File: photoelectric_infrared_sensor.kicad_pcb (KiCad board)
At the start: 4 copper layers, 121.1 x 63 mm, 38 parts

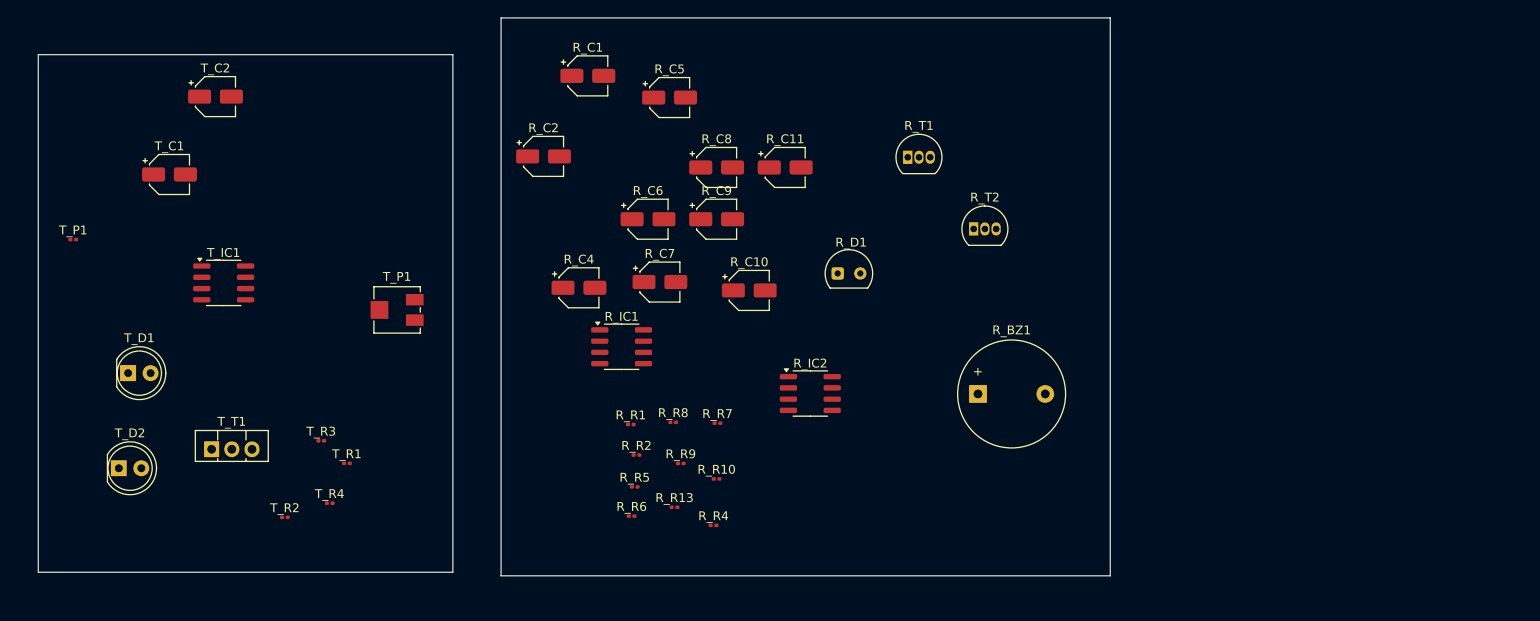
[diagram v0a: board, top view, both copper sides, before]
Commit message: added BOM
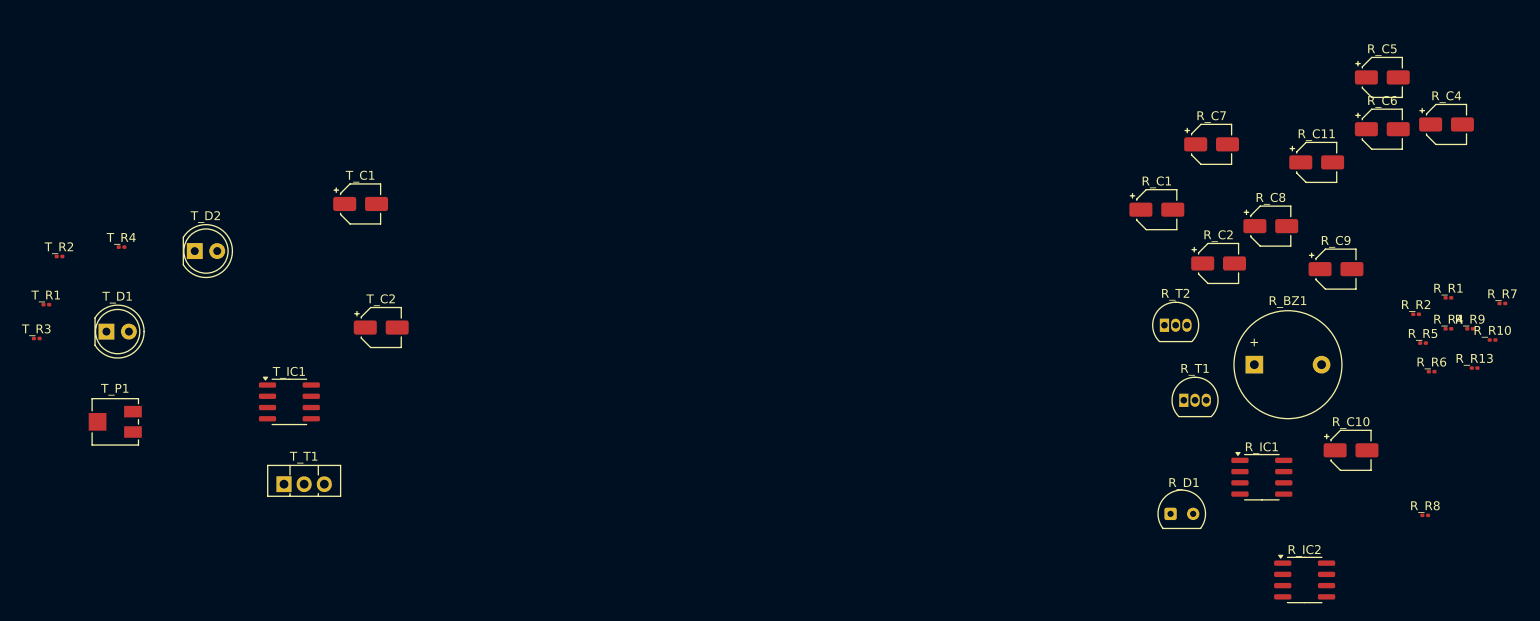
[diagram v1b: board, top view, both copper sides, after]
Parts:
- removed the T_P1 at (21.1, 58.5)
- removed the T_P1 at (57.8, 66.5)
- added T_P1: 10k, Potentiometer_SMD:Potentiometer_Vishay_TS53YJ_Vertical, F.Cu at (25.9, 79.2)
- R_IC1: value NE567 -> NE567_custom
- R_IC2: value NE555D -> NE555D_custom
- T_IC1: value TLC555xD -> TLC555xD_custom
- moved R_C4 99.8 mm to (176.3, 45.5)
- moved R_R1 93.5 mm to (176.6, 65.1)
- moved R_R6 91.9 mm to (174.7, 73.5)
- moved R_R13 91.8 mm to (179.5, 73.1)
- moved R_R5 90.6 mm to (173.7, 70.2)
- moved R_R9 90.5 mm to (179.0, 68.6)
- moved R_R7 89.7 mm to (182.7, 65.8)
- moved R_R2 89.5 mm to (172.9, 67.0)
- moved R_R10 89.1 mm to (181.6, 69.9)
- moved R_R4 86.0 mm to (176.6, 68.6)
- moved R_R8 85.6 mm to (173.9, 89.7)
- moved R_C6 83.6 mm to (169.1, 46.1)
- moved R_C5 80.6 mm to (169.1, 40.2)
- moved R_C2 77.2 mm to (150.6, 61.2)
- moved R_IC1 73.8 mm to (155.5, 85.4)
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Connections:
- net Net-(R_D1-K) renamed /R_LED
- net Net-(R_IC1-C3) renamed /R_C3
- net Net-(R_IC1-RC) renamed /R_RC
- net Net-(R_IC2-DIS) renamed /R_DIS
- net Net-(R_T1-C) renamed /R_BASE2
- net Net-(R_T2-E) renamed /R_EMITTER2
- net Net-(T_D1-A) renamed /T_LED1
- net Net-(T_D1-K) renamed /T_LED2
- net Net-(T_T1-B) renamed /T_BASE
- net Net-(T_T1-C) renamed /T_EMITTER
- net R_C2 renamed /R_C2
- net R_CV renamed /R_CV
- net R_IN renamed /R_IN
- net R_OUT1 renamed /R_OUT1
- net R_OUT2 renamed /R_OUT2
- net R_R renamed /R_R
- net R_TR renamed /R_THR/TR
- net T_DIS renamed /T_DIS
- net T_OUT renamed /T_OUT
- net T_THR renamed /T_THR/TR
- T_R1 pad 2: Net-(T_P1-Pad1) -> /T_POT
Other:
- board outline removed

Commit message: finished schematics
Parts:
- R_BZ1: footprint Buzzer_Beeper:Buzzer_12x9.5RM7.6 -> CPT-1203-03-SMT-TR:CPT-1203-03-SMT-TR
- R_C1, R_C10, R_C2, R_C4, R_C5, R_C8, R_C9, T_C1: footprint Capacitor_SMD:CP_Elec_4x3 -> Capacitor_SMD:C_0402_1005Metric_Pad0.74x0.62mm_HandSolder
- R_D1: value SFH205F -> BPW34; footprint OptoDevice:Osram_SFH205 -> BPW_34_FAS-Z:BPW34FASZ
- R_R1, R_R10, R_R13, R_R2, R_R4, R_R5, R_R6, R_R7, R_R8, R_R9, T_R1, T_R2, T_R3: footprint Resistor_SMD:R_0201_0603Metric -> ERJUP6:ERJUP6
- T_C2: footprint Capacitor_SMD:CP_Elec_4x3 -> Capacitor_SMD:CP_Elec_3x5.4
- T_D1, T_D2: value LD271 -> SFH 4851; footprint LED_THT:LED_D5.0mm_IRGrey -> SFH_4851:SFH4851
- T_P1: value 10k -> PVG5A103C03R00; footprint Potentiometer_SMD:Potentiometer_Vishay_TS53YJ_Vertical -> PVG5A103C03R00:PVG5A100C03R00
- T_R4: footprint Resistor_SMD:R_0201_0603Metric -> ERJS1T_U1T__2512_:ERJS1T_U1T__2512_
- T_T1: value BD140 -> BD136
- moved R_IC2 81.9 mm to (242.0, 91.0)
- moved R_IC1 74.0 mm to (229.3, 91.1)
- moved T_IC1 55.0 mm to (100.5, 78.7)
- moved T_R4 50.7 mm to (71.5, 82.9)
- moved T_P1 37.3 mm to (61.9, 88.8)
- moved R_BZ1 35.7 mm to (190.3, 73.6)
- moved T_D1 35.4 mm to (59.5, 76.3)
- moved T_D2 35.1 mm to (68.4, 70.0)
- moved R_C4 31.6 mm to (207.0, 53.2)
- moved R_D1 31.6 mm to (175.8, 97.2)
- moved R_R2 31.6 mm to (203.6, 74.7)
- moved R_R5 31.6 mm to (204.4, 78.0)
- moved R_R6 31.6 mm to (205.3, 81.2)
- moved R_R7 31.6 mm to (213.3, 73.5)
- moved R_R8 31.6 mm to (204.6, 97.4)
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
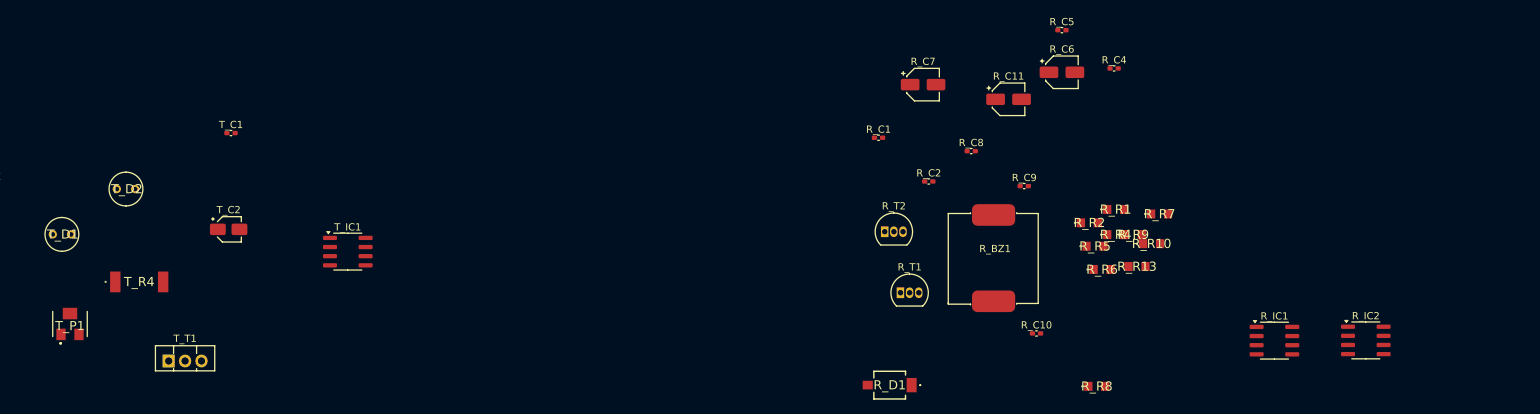
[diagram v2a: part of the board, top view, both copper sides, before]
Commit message: added schematics as .pdf
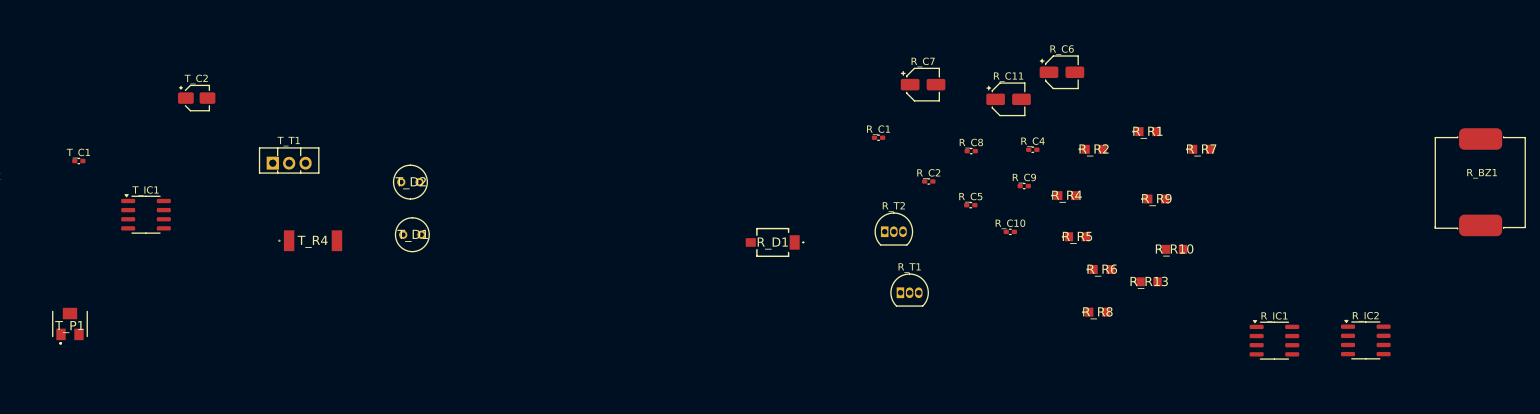
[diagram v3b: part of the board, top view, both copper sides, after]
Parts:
- moved R_BZ1 68.5 mm to (257.9, 63.0)
- moved T_D1 48.7 mm to (108.2, 76.3)
- moved T_D2 39.5 mm to (108.0, 69.0)
- moved T_T1 31.1 mm to (90.1, 66.4)
- moved T_IC1 28.5 mm to (72.5, 73.6)
- moved R_C5 27.4 mm to (187.1, 72.2)
- moved R_D1 25.6 mm to (159.6, 77.4)
- moved T_R4 24.8 mm to (95.7, 77.2)
- moved T_C1 21.5 mm to (63.2, 66.1)
- moved T_C2 18.8 mm to (79.5, 57.4)
- moved R_C4 16.0 mm to (195.7, 64.5)
- moved R_C10 14.6 mm to (192.6, 76.0)
- moved R_R1 11.7 mm to (211.7, 62.0)
- moved R_R7 10.7 mm to (219.2, 64.5)
- moved R_R8 10.3 mm to (204.7, 87.1)
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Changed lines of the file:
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@@
 	(footprint "ERJUP6:ERJUP6"
 		(layer "F.Cu")
-		(at 209.685 76.335)
+		(at 212.935 71.38)
 		(descr "ERJUP6")
 		(tags "Resistor")
@@
 	(footprint "ERJUP6:ERJUP6"
 		(layer "F.Cu")
-		(at 212.225 77.6)
+		(at 215.395 78.38)
 		(descr "ERJUP6")
 		(tags "Resistor")
@@
 	(footprint "ERJUP6:ERJUP6"
 		(layer "F.Cu")
-		(at 204.615 97.42)
+		(at 204.735 87.11)
 		(descr "ERJUP6")
 		(tags "Resistor")
@@
 	(footprint "Capacitor_SMD:C_0402_1005Metric_Pad0.74x0.62mm_HandSolder"
 		(layer "F.Cu")
-		(at 196.23 90.07)
+		(at 192.5925 75.95)
 		(descr "Capacitor SMD 0402 (1005 Metric), square (rectangular) end terminal, IPC_7351 nominal with elongated pad for handsoldering. (Body size source: IPC-SM-782 page 76, https://www.pcb-3d.com/wordpress/wp-content/uploads/ipc-sm-782a_amendment_1_and_2.pdf), generated with kicad-footprint-generator")
 		(tags "capacitor handsolder")
@@
 	(footprint "ERJUP6:ERJUP6"
 		(layer "F.Cu")
-		(at 213.335 73.47)
+		(at 219.175 64.48)
 		(descr "ERJUP6")
 		(tags "Resistor")
@@
 	(footprint "Capacitor_SMD:C_0402_1005Metric_Pad0.74x0.62mm_HandSolder"
 		(layer "F.Cu")
-		(at 84.295 62.225)
+		(at 63.1525 66.11)
 		(descr "Capacitor SMD 0402 (1005 Metric), square (rectangular) end terminal, IPC_7351 nominal with elongated pad for handsoldering. (Body size source: IPC-SM-782 page 76, https://www.pcb-3d.com/wordpress/wp-content/uploads/ipc-sm-782a_amendment_1_and_2.pdf), generated with kicad-footprint-generator")
 		(tags "capacitor handsolder")
@@
 	(footprint "ERJUP6:ERJUP6"
 		(layer "F.Cu")
-		(at 210.195 80.77)
+		(at 211.875 82.89)
 		(descr "ERJUP6")
 		(tags "Resistor")
@@
 	(footprint "Package_TO_SOT_THT:TO-126-3_Vertical"
 		(layer "F.Cu")
-		(at 75.635 93.895)
+		(at 90.1 66.41)
 		(descr "TO-126-3, Vertical, RM 2.28mm, see https://www.diodes.com/assets/Package-Files/TO126.pdf")
 		(tags "TO-126-3 Vertical RM 2.28mm")
@@
 	(footprint "SFH_4851:SFH4851"
 		(layer "F.Cu")
-		(at 68.43 70)
+		(at 107.96 69.04)
 		(descr "SFH 4851-3")
 		(tags "LED")
@@
 	(footprint "BPW_34_FAS-Z:BPW34FASZ"
 		(layer "F.Cu")
-		(at 175.83 97.25)
+		(at 159.58 77.42)
 		(descr "BPW 34 FAS-Z-3")
 		(tags "LED")
@@
 	(footprint "CPT-1203-03-SMT-TR:CPT-1203-03-SMT-TR"
 		(layer "F.Cu")
-		(at 190.27 73.6)
+		(at 257.95 63.05)
 		(property "Reference" "R_BZ1"
 			(at 0.2 4.7 0)
@@
 	(footprint "ERJUP6:ERJUP6"
 		(layer "F.Cu")
-		(at 203.585 74.69)
+		(at 204.235 64.48)
 		(descr "ERJUP6")
 		(tags "Resistor")
@@
 	(footprint "Capacitor_SMD:C_0402_1005Metric_Pad0.74x0.62mm_HandSolder"
 		(layer "F.Cu")
-		(at 199.765 47.925)
+		(at 187.0975 72.24)
 		(descr "Capacitor SMD 0402 (1005 Metric), square (rectangular) end terminal, IPC_7351 nominal with elongated pad for handsoldering. (Body size source: IPC-SM-782 page 76, https://www.pcb-3d.com/wordpress/wp-content/uploads/ipc-sm-782a_amendment_1_and_2.pdf), generated with kicad-footprint-generator")
 		(tags "capacitor handsolder")
@@
 	(footprint "Capacitor_SMD:C_0402_1005Metric_Pad0.74x0.62mm_HandSolder"
 		(layer "F.Cu")
-		(at 207.02 53.24)
+		(at 195.7175 64.54)
 		(descr "Capacitor SMD 0402 (1005 Metric), square (rectangular) end terminal, IPC_7351 nominal with elongated pad for handsoldering. (Body size source: IPC-SM-782 page 76, https://www.pcb-3d.com/wordpress/wp-content/uploads/ipc-sm-782a_amendment_1_and_2.pdf), generated with kicad-footprint-generator")
 		(tags "capacitor handsolder")
@@
 	(footprint "ERJUP6:ERJUP6"
 		(layer "F.Cu")
-		(at 207.235 72.835)
+		(at 211.705 62.02)
 		(descr "ERJUP6")
 		(tags "Resistor")
@@
 	(footprint "SFH_4851:SFH4851"
 		(layer "F.Cu")
-		(at 59.53 76.3)
+		(at 108.23 76.35)
 		(descr "SFH 4851-3")
 		(tags "LED")
@@
 	(footprint "ERJUP6:ERJUP6"
 		(layer "F.Cu")
-		(at 204.365 77.95)
+		(at 201.915 76.63)
 		(descr "ERJUP6")
 		(tags "Resistor")
@@
 	(footprint "Package_SO:SOIC-8_3.9x4.9mm_P1.27mm"
 		(layer "F.Cu")
-		(at 100.525 78.695)
+		(at 72.485 73.565)
 		(descr "SOIC, 8 Pin (JEDEC MS-012AA, https://www.analog.com/media/en/package-pcb-resources/package/pkg_pdf/soic_narrow-r/r_8.pdf), generated with kicad-footprint-generator ipc_gullwing_generator.py")
 		(tags "SOIC SO")
@@
 	(footprint "Capacitor_SMD:CP_Elec_3x5.4"
 		(layer "F.Cu")
-		(at 83.97 75.6)
+		(at 79.53 57.36)
 		(descr "SMD capacitor, aluminum electrolytic, Nichicon, 3.0x5.4mm")
 		(tags "capacitor electrolytic")
@@
 	(footprint "ERJS1T_U1T__2512_:ERJS1T_U1T__2512_"
 		(layer "F.Cu")
-		(at 71.545 82.9)
+		(at 95.695 77.18)
 		(descr "ERJS1T_U1T_(2512)")
 		(tags "Resistor")
@@
 	(footprint "ERJUP6:ERJUP6"
 		(layer "F.Cu")
-		(at 207.235 76.335)
+		(at 200.435 70.91)
 		(descr "ERJUP6")
 		(tags "Resistor")
